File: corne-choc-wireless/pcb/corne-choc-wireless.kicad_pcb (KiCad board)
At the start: 2 copper layers, 275.5 x 105.6 mm, 172 parts, among them J1 MJ-4PP-9, J2 OLED, J3 MJ-4PP-9, J4 OLED, SW1 SW_PUSH, SW10 SW_PUSH, SW11 SW_PUSH, SW12 SW_PUSH, SW13 SW_PUSH, SW14 SW_PUSH, SW15 SW_PUSH, SW16 SW_PUSH, SW17 SW_PUSH, SW18 SW_PUSH, SW19 SW_PUSH, SW2 SW_PUSH, SW20 SW_PUSH, SW21 SW_PUSH, SW22 SW_PUSH, SW23 SW_PUSH, SW24 SW_PUSH, SW25 SW_PUSH, SW26 SW_PUSH, SW27 SW_PUSH, SW28 SW_PUSH, SW29 SW_PUSH, SW3 SW_PUSH, SW30 SW_PUSH, SW31 SW_PUSH, SW32 SW_PUSH, SW33 SW_PUSH, SW34 SW_PUSH, SW35 SW_PUSH, SW36 SW_PUSH, SW37 SW_PUSH, SW38 SW_PUSH, SW39 SW_PUSH, SW4 SW_PUSH, SW40 SW_PUSH, SW41 SW_PUSH, SW42 SW_PUSH, SW5 SW_PUSH, SW6 SW_PUSH, SW7 SW_PUSH, SW8 SW_PUSH, SW9 SW_PUSH, U1 ProMicro, U2 ProMicro

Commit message: move things to the right place
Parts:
- removed G*** (x4): LOGO, kbd:corne-logo-horizontal
- removed J1, J3: MJ-4PP-9, kbd:MJ-4PP-9_1side
- removed LED1, LED2, LED28, LED29, LED3, LED30, LED31, LED32, LED33, LED4, LED5, LED6: WS2812B, LED_SMD:LED_WS2812B_PLCC4_5.0x5.0mm_P3.2mm
- removed LED10, LED11, LED12, LED13, LED14, LED15, LED16, LED17, LED18, LED19, LED20, LED21, LED22, LED23, LED24, LED25, LED26, LED27, LED34, LED35, LED36, LED37, LED38, LED39, LED40, LED41, LED42, LED43, LED44, LED45, LED46, LED47, LED48, LED49, LED50, LED51, LED52, LED53, LED54, LED7, LED8, LED9: YS-SK6812MINI-E, kbd:YS-SK6812MINI-E
- removed Ref** (x14): Val**, kbd:M2_HOLE_v2
- removed SW28, SW7: SW_PUSH, kbd:CherryMX_Hotswap
- added BATJ1: Conn_01x02_Socket, Connector_PinHeader_2.54mm:PinHeader_1x02_P2.54mm_Vertical, F.Cu at (96.6, -55.7)
- added BATJ2: Conn_01x02_Socket, Connector_JST:JST_PH_S2B-PH-K_1x02_P2.00mm_Horizontal, F.Cu at (129.9, -60.5)
- added BATJ3: Conn_01x02_Socket, Connector_PinHeader_2.54mm:PinHeader_1x02_P2.54mm_Vertical, F.Cu at (222.3, -34.4)
- added BATJ4: Conn_01x02_Socket, Connector_JST:JST_PH_S2B-PH-K_1x02_P2.00mm_Horizontal, F.Cu at (180.5, -57.0)
- added L_ENC1: RollerEncoder_EVQWGD001, zzkeeb:RotaryEncoder_EVQWGD001, F.Cu at (64.6, -51.7)
- added PSW1: SW_SPDT, Button_Switch_SMD:SW_SPDT_PCM12, F.Cu at (120.7, -29.6)
- added PSW_r1: SW_SPDT, Button_Switch_SMD:SW_SPDT_PCM12, F.Cu at (174.5, -39.9)
- added R_ENC1: RollerEncoder_EVQWGD001, zzkeeb:RotaryEncoder_EVQWGD001, F.Cu at (299.9, -53.2)
- J2, J4: value OLED -> Nice!View; footprint kbd:OLED_1side -> niceview:nice_view_1side
- U1, U2: value ProMicro -> Nice!Nano
- locked: renamed from REF**; value Breakaway_Tabs -> locked
- moved RSW1 10.4 mm to (145.1, 76.6)
- moved D29 10.4 mm to (267.5, 64.9)
- moved D22 10.4 mm to (286.5, 45.9)
- moved D23 10.4 mm to (267.5, 45.9)
- moved D28 10.4 mm to (286.5, 64.8)
- moved D34 10.4 mm to (286.5, 83.9)
- moved D35 10.4 mm to (267.5, 83.9)
- moved D24 10.4 mm to (248.5, 41.2)
- moved D25 10.4 mm to (229.5, 38.8)
- moved D26 10.4 mm to (210.5, 41.2)
- moved D27 10.4 mm to (191.5, 43.5)
- moved D30 10.4 mm to (248.5, 60.2)
- moved D31 10.4 mm to (229.5, 57.8)
- moved D32 10.4 mm to (210.5, 60.2)
- moved D33 10.4 mm to (191.5, 62.5)
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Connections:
- net col0 renamed L_Enc_1
- net col0_r renamed R_Enc_1
- D28 pad 2: Net-(D28-Pad2) -> R_Enc_2
- D7 pad 2: Net-(D7-Pad2) -> L_Enc_2
- U1 pad 1: LED -> unconnected-(U1-D1-Pad1)
- U1 pad 11: Net-(U1-Pad11) -> unconnected-(U1-D8-Pad11)
- U1 pad 12: Net-(U1-Pad12) -> unconnected-(U1-D9-Pad12)
- U1 pad 13: Net-(U1-Pad13) -> L_ENC_B
- U1 pad 14: Net-(U1-Pad14) -> L_ENC_A
- U1 pad 2: data -> CS
- U1 pad 24: Net-(U1-Pad24) -> +BATT
- U2 pad 1: LED_r -> unconnected-(U2-D1-Pad1)
- U2 pad 11: Net-(U2-Pad11) -> unconnected-(U2-D8-Pad11)
- U2 pad 12: Net-(U2-Pad12) -> unconnected-(U2-D9-Pad12)
- U2 pad 13: Net-(U2-Pad13) -> R_ENC_B
- U2 pad 14: Net-(U2-Pad14) -> R_ENC_A
- U2 pad 2: data_r -> CS_r
- U2 pad 24: Net-(U2-Pad24) -> +BATTA
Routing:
- net GND: track 637.2 -> 49.8 mm, vias 16 -> 0
- net GNDA: track 617.9 -> 78.0 mm, vias 15 -> 0
- net VDD: track 573.1 -> 37.5 mm, vias 2 -> 0
- net VCC: track 544.3 -> 37.3 mm, vias 2 -> 0
- net data: track 77.0 -> 0.00 mm
- net Net-(LED31-Pad2): track 71.8 -> 0.00 mm, vias 2 -> 0
- net data_r: track 62.9 -> 0.00 mm
- net Net-(LED1-Pad4): track 47.8 -> 0.00 mm
- net Net-(LED32-Pad2): track 47.4 -> 0.00 mm
- net Net-(LED2-Pad4): track 46.3 -> 0.00 mm
- net Net-(LED4-Pad2): track 43.6 -> 0.00 mm, vias 2 -> 0
- net Net-(LED28-Pad2): track 41.5 -> 0.00 mm, vias 2 -> 0
- net LED: track 41.1 -> 0.00 mm
- net Net-(LED20-Pad4): track 36.8 -> 0.00 mm, vias 4 -> 0
- net Net-(LED29-Pad4): track 36.4 -> 0.00 mm
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
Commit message: Readd screw holes
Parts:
- added ?: , , F.Cu at (50.6, 74.6)
- added ?: , , F.Cu at (269.0, 55.6)
- added ?: , , F.Cu at (129.8, 84.6)
- added ?: , , F.Cu at (50.6, 55.6)
- added ?: , , F.Cu at (193.1, 52.1)
- added ?: , , F.Cu at (250.1, 74.6)
- added ?: , , F.Cu at (121.3, 99.5)
- added ?: , , F.Cu at (170.7, 84.7)
- added ?: , , F.Cu at (107.5, 52.1)
- added ?: , , F.Cu at (269.0, 74.6)
- added ?: , , F.Cu at (156.2, 93.2)
- added ?: , , F.Cu at (74.7, 91.8)
- added ?: , , F.Cu at (144.2, 93.1)
- added ?: , , F.Cu at (179.3, 99.6)
- added ?: , , F.Cu at (250.1, 55.6)
- added ?: , , F.Cu at (31.5, 55.6)
- added ?: , , F.Cu at (31.5, 74.6)
- added ?: , , F.Cu at (225.9, 91.8)
- moved BATJ1 134.0 mm to (135.6, 72.5), turned to 90 degrees
- moved PSW_r1 126.8 mm to (156.4, 85.6), turned to -90 degrees
- moved BATJ3 121.1 mm to (165.4, 72.5), turned to -90 degrees
- moved PSW1 117.7 mm to (144.7, 85.6), turned to 90 degrees

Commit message: Fix edge cuts
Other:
- outline, holes or cut-outs redrawn

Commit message: Fix holes
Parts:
- removed the ? at (269.0, 55.6)
- removed the ? at (193.1, 52.1)
- removed the ? at (250.1, 74.6)
- removed the ? at (170.7, 84.7)
- removed the ? at (269.0, 74.6)
- removed the ? at (156.2, 93.2)
- removed the ? at (179.3, 99.6)
- removed the ? at (250.1, 55.6)
- removed the ? at (225.9, 91.8)
- added ?: , , B.Cu at (179.6, 99.3)
- added ?: , , B.Cu at (193.4, 51.9)
- added ?: , , B.Cu at (171.1, 84.4)
- added ?: , , B.Cu at (269.3, 55.4)
- added ?: , , B.Cu at (226.2, 91.7)
- added ?: , , B.Cu at (156.7, 92.9)
- added ?: , , B.Cu at (250.3, 74.4)
- added ?: , , B.Cu at (250.3, 55.4)
- added ?: , , B.Cu at (269.3, 74.4)
- moved ? 0.23 mm to (144.4, 92.9)
- moved ? 0.23 mm to (130.0, 84.4)
- moved ? 0.23 mm to (121.4, 99.3)
- moved ? 0.23 mm to (50.7, 55.4)
- moved ? 0.23 mm to (74.9, 91.7)
- moved ? 0.23 mm to (107.7, 51.9)
- moved ? 0.23 mm to (50.7, 74.4)
- moved ? 0.23 mm to (31.7, 55.4)
- moved ? 0.23 mm to (31.7, 74.4)

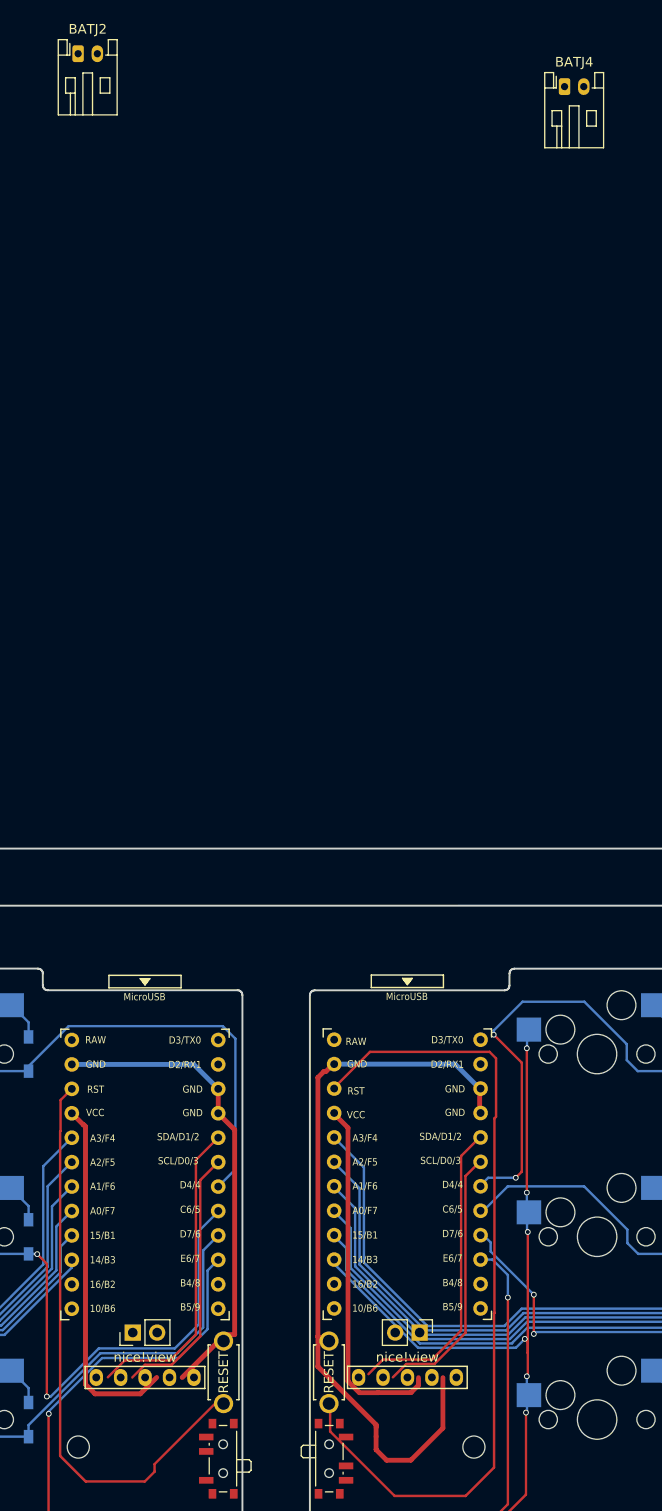
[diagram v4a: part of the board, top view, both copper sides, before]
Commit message: Fix holes
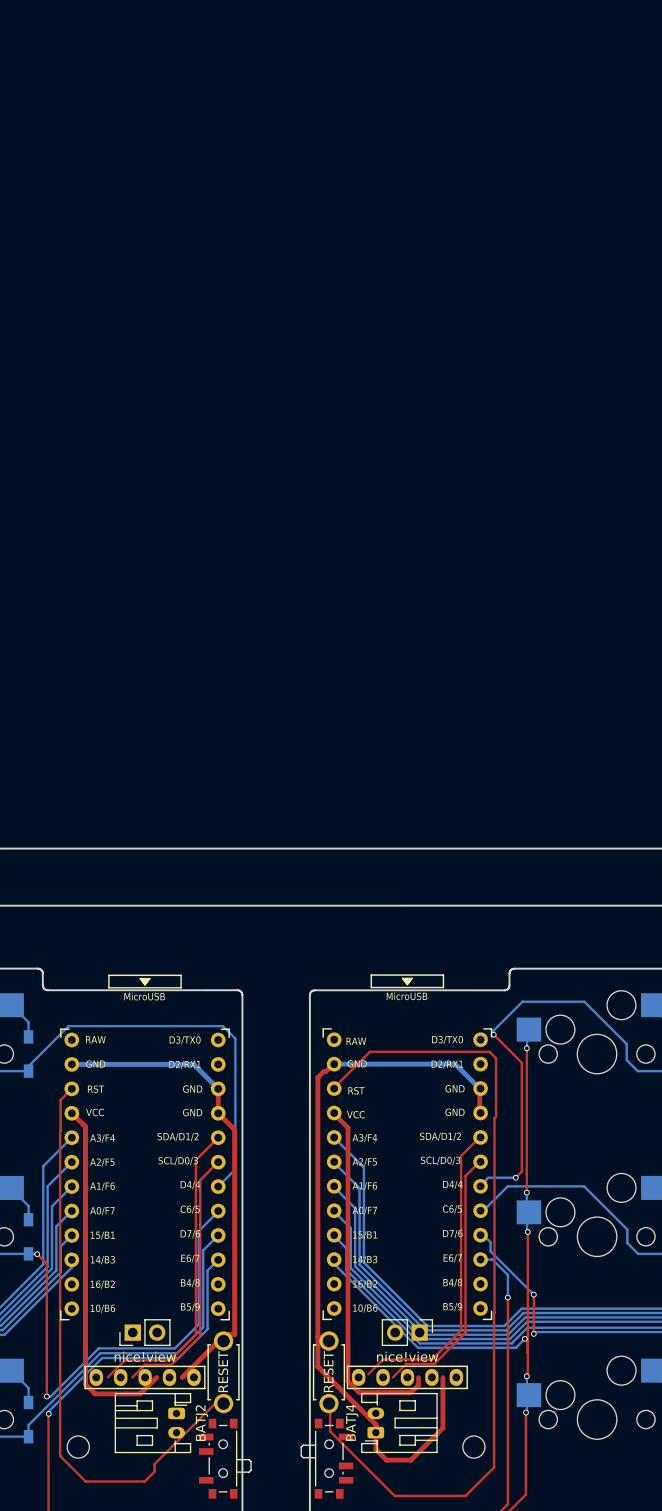
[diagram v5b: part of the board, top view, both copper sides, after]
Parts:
- moved BATJ2 141.7 mm to (140.2, 80.9), turned to -90 degrees
- moved BATJ4 141.3 mm to (160.9, 82.9), turned to 90 degrees
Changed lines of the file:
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@@
   )
   (footprint "Connector_JST:JST_PH_S2B-PH-K_1x02_P2.00mm_Horizontal" (layer "F.Cu")
-    (at 129.9375 -60.45)
+    (at 140.17 80.91 -90)
     (descr "JST PH series connector, S2B-PH-K (http://www.jst-mfg.com/product/pdf/eng/ePH.pdf), generated with kicad-footprint-generator")
     (tags "connector JST PH top entry")
@@
     (property "ki_keywords" "connector")
     (attr through_hole)
-    (fp_text reference "BATJ2" (at 1 -2.55) (layer "F.SilkS")
+    (fp_text reference "BATJ2" (at 1 -2.55 90) (layer "F.SilkS")
         (effects (font (size 1 1) (thickness 0.15)))
     )
-    (fp_text value "Conn_01x02_Socket" (at 1 7.45) (layer "F.Fab")
+    (fp_text value "Conn_01x02_Socket" (at 1 7.45 90) (layer "F.Fab")
         (effects (font (size 1 1) (thickness 0.15)))
     )
-    (fp_text user "${REFERENCE}" (at 1 2.5) (layer "F.Fab")
+    (fp_text user "${REFERENCE}" (at 1 2.5 90) (layer "F.Fab")
         (effects (font (size 1 1) (thickness 0.15)))
     )
@@
     (fp_line (start 3.95 6.25) (end 3.95 -1.35)
       (stroke (width 0.1) (type solid)) (layer "F.Fab"))
-    (pad "1" thru_hole roundrect (at 0 0) (size 1.2 1.75) (drill 0.75) (layers "*.Cu" "*.Mask") (roundrect_rratio 0.208333)
+    (pad "1" thru_hole roundrect (at 0 0 270) (size 1.2 1.75) (drill 0.75) (layers "*.Cu" "*.Mask") (roundrect_rratio 0.208333)
       (net 2 "Net-(BATJ1-Pin_2)") (pinfunction "Pin_1") (pintype "passive"))
-    (pad "2" thru_hole oval (at 2 0) (size 1.2 1.75) (drill 0.75) (layers "*.Cu" "*.Mask")
+    (pad "2" thru_hole oval (at 2 0 270) (size 1.2 1.75) (drill 0.75) (layers "*.Cu" "*.Mask")
       (net 26 "GND") (pinfunction "Pin_2") (pintype "passive"))
     (model "${KICAD6_3DMODEL_DIR}/Connector_JST.3dshapes/JST_PH_S2B-PH-K_1x02_P2.00mm_Horizontal.wrl"
@@
   )
   (footprint "Connector_JST:JST_PH_S2B-PH-K_1x02_P2.00mm_Horizontal" (layer "F.Cu")
-    (at 180.5075 -57.03)
+    (at 160.89 82.9 90)
     (descr "JST PH series connector, S2B-PH-K (http://www.jst-mfg.com/product/pdf/eng/ePH.pdf), generated with kicad-footprint-generator")
     (tags "connector JST PH top entry")
@@
     (property "ki_keywords" "connector")
     (attr through_hole)
-    (fp_text reference "BATJ4" (at 1 -2.55) (layer "F.SilkS")
+    (fp_text reference "BATJ4" (at 1 -2.55 90) (layer "F.SilkS")
         (effects (font (size 1 1) (thickness 0.15)))
     )
-    (fp_text value "Conn_01x02_Socket" (at 1 7.45) (layer "F.Fab")
+    (fp_text value "Conn_01x02_Socket" (at 1 7.45 90) (layer "F.Fab")
         (effects (font (size 1 1) (thickness 0.15)))
     )
-    (fp_text user "${REFERENCE}" (at 1 2.5) (layer "F.Fab")
+    (fp_text user "${REFERENCE}" (at 1 2.5 90) (layer "F.Fab")
         (effects (font (size 1 1) (thickness 0.15)))
     )
@@
     (fp_line (start 3.95 6.25) (end 3.95 -1.35)
       (stroke (width 0.1) (type solid)) (layer "F.Fab"))
-    (pad "1" thru_hole roundrect (at 0 0) (size 1.2 1.75) (drill 0.75) (layers "*.Cu" "*.Mask") (roundrect_rratio 0.208333)
+    (pad "1" thru_hole roundrect (at 0 0 90) (size 1.2 1.75) (drill 0.75) (layers "*.Cu" "*.Mask") (roundrect_rratio 0.208333)
       (net 4 "Net-(BATJ3-Pin_2)") (pinfunction "Pin_1") (pintype "passive"))
-    (pad "2" thru_hole oval (at 2 0) (size 1.2 1.75) (drill 0.75) (layers "*.Cu" "*.Mask")
+    (pad "2" thru_hole oval (at 2 0 90) (size 1.2 1.75) (drill 0.75) (layers "*.Cu" "*.Mask")
       (net 81 "GNDA") (pinfunction "Pin_2") (pintype "passive"))
     (model "${KICAD6_3DMODEL_DIR}/Connector_JST.3dshapes/JST_PH_S2B-PH-K_1x02_P2.00mm_Horizontal.wrl"
@@
     (pad "" np_thru_hole circle (at 0 0) (size 4.3 4.3) (drill 4.3) (layers "F&B.Cu" "*.Mask"))
   )
-  (gr_curve (pts (xy 144.505353 72.420464) (xy 145.057634 72.420464) (xy 145.505348 72.868178) (xy 145.505348 73.420464))
-    (stroke (width 0.2) (type solid)) (layer "Dwgs.User"))
-  (gr_curve (pts (xy 156.375389 72.420464) (xy 156.92767 72.420464) (xy 157.375384 72.868178) (xy 157.375384 73.420464))
-    (stroke (width 0.2) (type solid)) (layer "Dwgs.User"))
-  (gr_curve (pts (xy 155.375394 73.420464) (xy 155.375394 72.868178) (xy 155.823108 72.420464) (xy 156.375389 72.420464))
-    (stroke (width 0.2) (type solid)) (layer "Dwgs.User"))
-  (gr_curve (pts (xy 144.505353 72.420464) (xy 145.057634 72.420464) (xy 145.505348 72.868178) (xy 145.505348 73.420464))
-    (stroke (width 0.2) (type solid)) (layer "Dwgs.User"))
-  (gr_curve (pts (xy 145.505348 73.420464) (xy 145.505348 73.97275) (xy 145.057634 74.420464) (xy 144.505353 74.420464))
-    (stroke (width 0.2) (type solid)) (layer "Dwgs.User"))
-  (gr_curve (pts (xy 144.505353 74.420464) (xy 143.953072 74.420464) (xy 143.505358 73.97275) (xy 143.505358 73.420464))
-    (stroke (width 0.2) (type solid)) (layer "Dwgs.User"))
-  (gr_curve (pts (xy 156.375389 74.420464) (xy 155.823108 74.420464) (xy 155.375394 73.97275) (xy 155.375394 73.420464))
-    (stroke (width 0.2) (type solid)) (layer "Dwgs.User"))
-  (gr_curve (pts (xy 145.505348 73.420464) (xy 145.505348 73.97275) (xy 145.057634 74.420464) (xy 144.505353 74.420464))
-    (stroke (width 0.2) (type solid)) (layer "Dwgs.User"))
-  (gr_curve (pts (xy 156.375389 74.420464) (xy 155.823108 74.420464) (xy 155.375394 73.97275) (xy 155.375394 73.420464))
-    (stroke (width 0.2) (type solid)) (layer "Dwgs.User"))
-  (gr_curve (pts (xy 157.375384 73.420464) (xy 157.375384 73.97275) (xy 156.92767 74.420464) (xy 156.375389 74.420464))
-    (stroke (width 0.2) (type solid)) (layer "Dwgs.User"))
-  (gr_curve (pts (xy 157.375384 73.420464) (xy 157.375384 73.97275) (xy 156.92767 74.420464) (xy 156.375389 74.420464))
-    (stroke (width 0.2) (type solid)) (layer "Dwgs.User"))
-  (gr_curve (pts (xy 156.375389 72.420464) (xy 156.92767 72.420464) (xy 157.375384 72.868178) (xy 157.375384 73.420464))
-    (stroke (width 0.2) (type solid)) (layer "Dwgs.User"))
-  (gr_curve (pts (xy 155.375394 73.420464) (xy 155.375394 72.868178) (xy 155.823108 72.420464) (xy 156.375389 72.420464))
-    (stroke (width 0.2) (type solid)) (layer "Dwgs.User"))
-  (gr_curve (pts (xy 143.505358 73.420464) (xy 143.505358 72.868178) (xy 143.953072 72.420464) (xy 144.505353 72.420464))
-    (stroke (width 0.2) (type solid)) (layer "Dwgs.User"))
-  (gr_curve (pts (xy 144.505353 74.420464) (xy 143.953072 74.420464) (xy 143.505358 73.97275) (xy 143.505358 73.420464))
-    (stroke (width 0.2) (type solid)) (layer "Dwgs.User"))
-  (gr_curve (pts (xy 143.505358 73.420464) (xy 143.505358 72.868178) (xy 143.953072 72.420464) (xy 144.505353 72.420464))
-    (stroke (width 0.2) (type solid)) (layer "Dwgs.User"))
   (gr_line (start 19.533493 94.261585) (end 19.528414 94.264125)
     (stroke (width 0.199999) (type solid)) (layer "Edge.Cuts"))

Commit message: All traces done
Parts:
- removed the ? at (50.7, 74.4)
- removed the ? at (250.3, 74.4)
- removed the ? at (250.3, 55.4)
- removed the ? at (50.7, 55.4)
- moved L_ENC1 123.7 mm to (21.5, 64.3)
- moved R_ENC1 120.2 mm to (279.2, 65.2), turned to 180 degrees
- moved D21 37.9 mm to (137.9, 101.0)
- moved D20 21.5 mm to (118.0, 104.3)
- moved D19 19.8 mm to (98.0, 98.8)
- moved D42 19.3 mm to (181.8, 107.2)
- moved D28 11.5 mm to (279.0, 73.5), turned to 0 degrees
- moved D7 0.18 mm to (29.9, 64.8)
- turned RSW1 to 90 degrees
- turned RSW2 to 90 degrees
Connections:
- U2 pad 11: unconnected-(U2-D8-Pad11) -> R_ENC_B
- U2 pad 12: unconnected-(U2-D9-Pad12) -> R_ENC_A
- U2 pad 13: R_ENC_B -> unconnected-(U2-D10-Pad13)
- U2 pad 14: R_ENC_A -> unconnected-(U2-D16-Pad14)
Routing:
- net GND: track 49.8 -> 200.3 mm
- net L_ENC_B: track 0.00 -> 119.2 mm
- net L_ENC_A: track 0.00 -> 118.0 mm
- net GNDA: track 78.0 -> 195.2 mm, vias 0 -> 2
- net R_ENC_B: track 0.00 -> 114.5 mm
- net R_ENC_A: track 0.00 -> 113.5 mm
- net row1: track 193.1 -> 125.6 mm, vias 2 -> 10
- net reset_r: track 85.1 -> 26.9 mm
- net row0_r: track 184.4 -> 129.2 mm, vias 2 -> 11
- net row0: track 182.7 -> 130.3 mm, vias 2 -> 10
- net +BATT: track 0.00 -> 51.0 mm
- net row1_r: track 166.2 -> 120.9 mm, vias 0 -> 11
- net +BATTA: track 0.00 -> 43.5 mm
- net row2: track 180.3 -> 140.8 mm, vias 2 -> 6
- net row2_r: track 172.0 -> 133.5 mm, vias 2 -> 6
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
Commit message: Tweak tracks
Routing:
- net row3_r: track 105.3 -> 109.8 mm, vias 2 -> 0
- net L_Enc_1: track 159.4 -> 158.0 mm
- net R_Enc_1: track 175.0 -> 174.1 mm
- net col2: track 118.6 -> 117.7 mm
- net GND: track 200.3 -> 199.5 mm
- net reset_r: track 26.9 -> 26.2 mm
- net col1: track 137.8 -> 137.0 mm
- net SDA: track 30.9 -> 30.2 mm
- net Net-(BATJ1-Pin_2): track 13.3 -> 12.7 mm
- net col4_r: track 108.7 -> 108.1 mm
- net row0: track 130.3 -> 129.7 mm
- net col5: track 96.1 -> 95.5 mm
- net col1_r: track 140.5 -> 140.0 mm
- net L_ENC_A: track 118.0 -> 117.5 mm
